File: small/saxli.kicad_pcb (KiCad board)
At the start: 4 copper layers, 160.5 x 102.4 mm, 206 parts, among them IC1 PIC32MX350F256H-V_PT, IC2 SIM808, J1 78800-0001, J10 Conn_01x06_Female, J11 Conn_Coaxial, J12 Conn_Coaxial, J2 Screw_Terminal_01x02, J3 Micro_SD_Card, J4 Conn_01x05_Female, J5 Conn_02x04_Odd_Even, J6 RJ45_Amphenol_RJMG1BD3B8K1ANR, J7 Screw_Terminal_01x08, J8 Screw_Terminal_01x08, J9 Screw_Terminal_01x08, Q1 2N7002, Q2 2N7002, Q3 2N7002, Q4 AO3401A, U1 LM358, U10 TPS5430DDAR, U11 EL357N(C)(TA)-G, U12 EL357N(C)(TA)-G, U13 ASSR-1218, U14 ST485EBDR, U15 ASSR-1218, U16 SRV05-4, U18 ULN2003A, U2 LM7805_TO220, U20 TPS5430DDAR, U4 ENC28J60x-SS, U5 AT25M02, U6 EL357N(C)(TA)-G, U7 EL357N(C)(TA)-G, U8 PCF8563T, U9 ISO1540, Y1 Crystal, Y2 Crystal

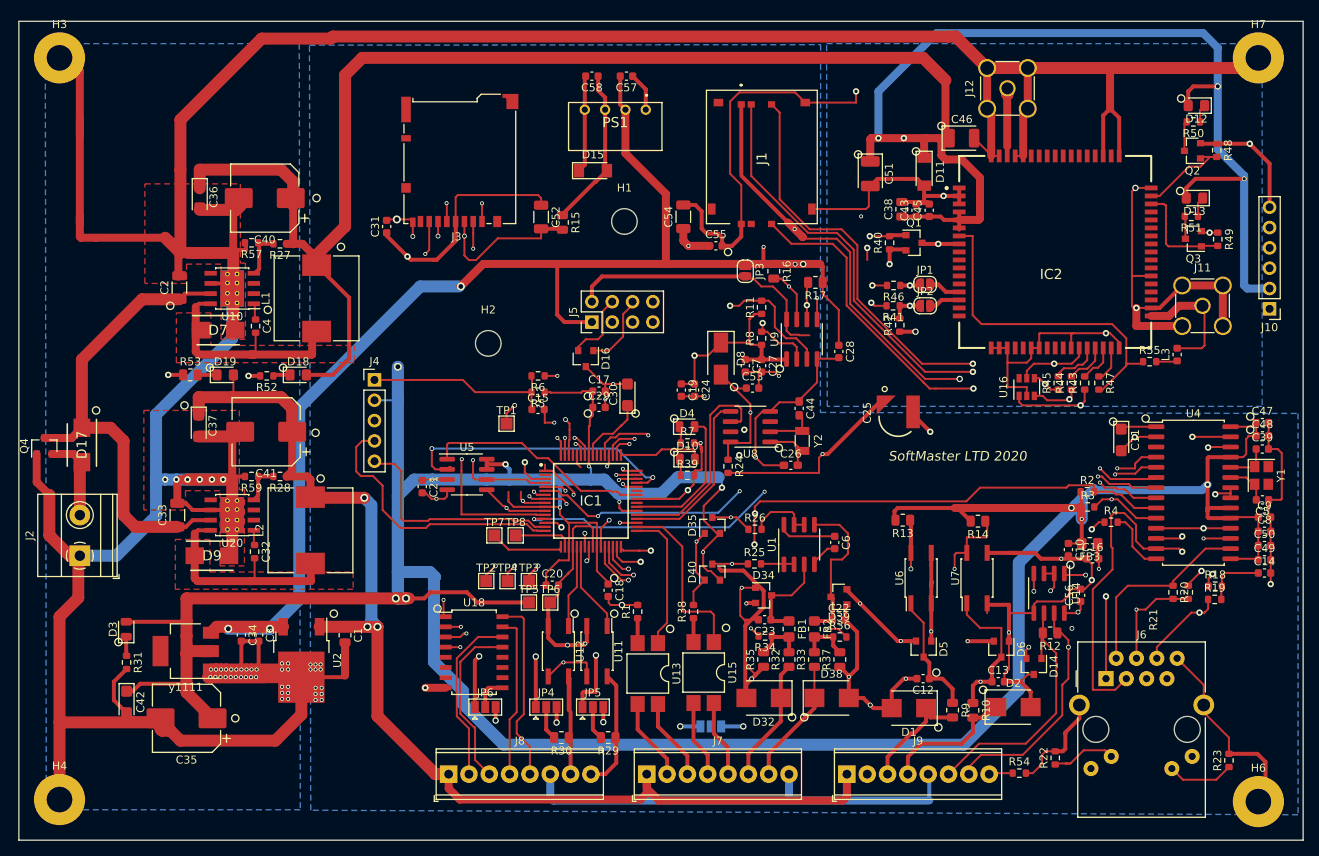
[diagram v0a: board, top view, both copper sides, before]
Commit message: JLCPCB orientation fixed
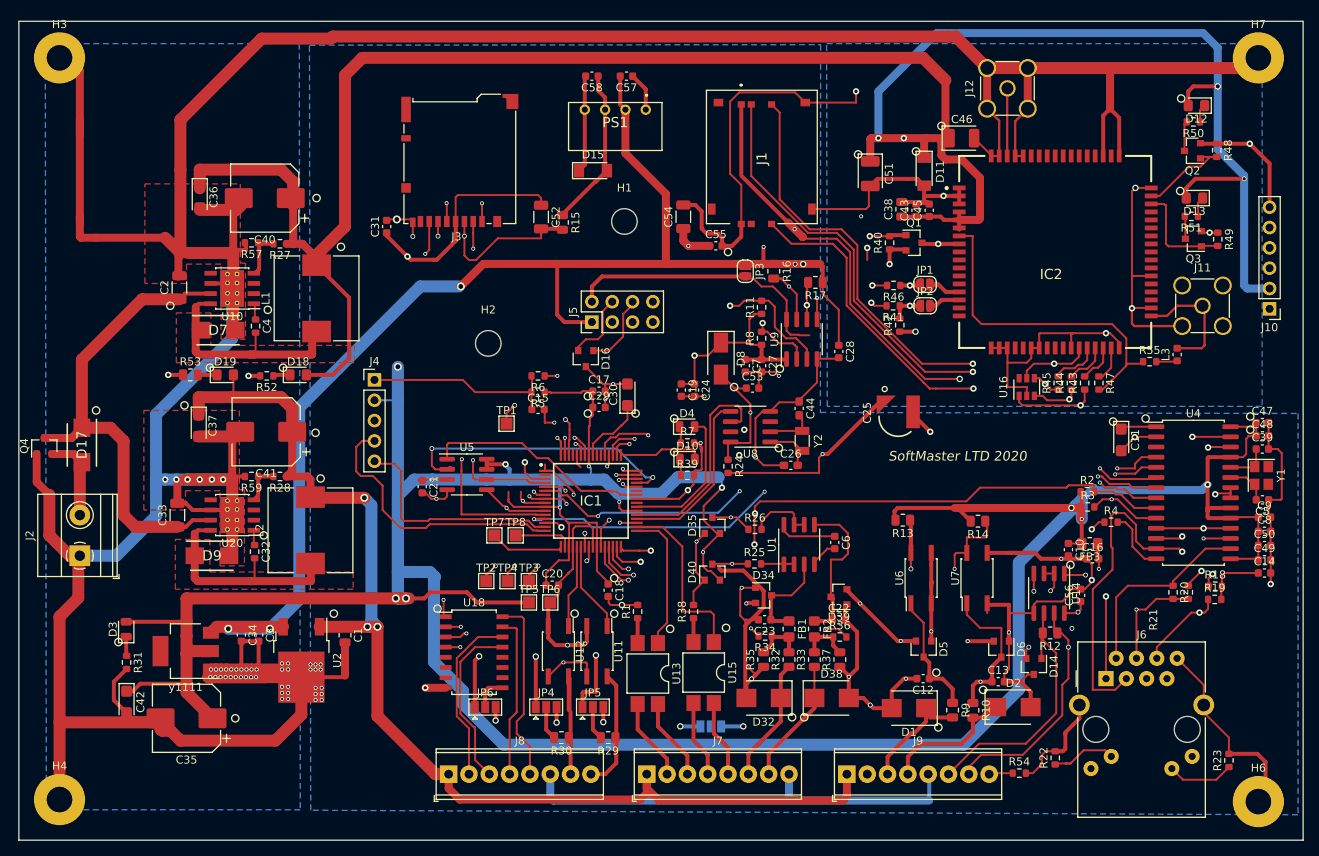
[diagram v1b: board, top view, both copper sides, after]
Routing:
- net GND: track 1217.8 -> 1193.0 mm
- net GSM_ANT: track 15.8 -> 8.46 mm
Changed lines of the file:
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@@
   (general
     (thickness 1.6)
-    (drawings 50)
-    (tracks 2536)
+    (drawings 51)
+    (tracks 2526)
     (zones 0)
     (modules 206)
@@
   (layers
     (0 F.Cu signal)
-    (1 In1.Cu signal)
-    (2 In2.Cu signal)
-    (31 B.Cu signal)
+    (1 In1.Cu signal hide)
+    (2 In2.Cu signal hide)
+    (31 B.Cu signal hide)
     (32 B.Adhes user)
     (33 F.Adhes user)
@@
   )
   (setup
-    (last_trace_width 0.25)
+    (last_trace_width 0.2933)
+    (user_trace_width 0.2933)
     (user_trace_width 0.5)
     (user_trace_width 1)
@@
     )
   )
+  (gr_circle (center 68.707 85.09) (end 68.453 84.709) (layer F.SilkS) (width 0.12))
   (gr_circle (center 133.223 64.262) (end 132.969 63.881) (layer F.SilkS) (width 0.12))
   (gr_circle (center 127.508 66.548) (end 127.254 66.167) (layer F.SilkS) (width 0.12))
@@
   (segment (start 187.833 36.132) (end 185.865 36.132) (width 0.25) (layer F.Cu) (net 1))
   (segment (start 177.785 56.657) (end 177.434 56.657) (width 0.25) (layer F.Cu) (net 1))
-  (via (at 177.785 56.657) (size 0.8) (drill 0.4) (layers F.Cu B.Cu) (net 1))
   (segment (start 162.64 37.657) (end 163.64 37.657) (width 0.25) (layer F.Cu) (net 1))
   (segment (start 149.098 40.526) (end 147.32 40.526) (width 0.5) (layer F.Cu) (net 1))
@@
   (segment (start 106.75 89.859) (end 106.693 89.916) (width 0.25) (layer F.Cu) (net 1))
   (segment (start 163.64 32.575) (end 164.465 31.75) (width 0.5) (layer F.Cu) (net 1))
-  (segment (start 163.64 37.657) (end 163.64 32.575) (width 0.5) (layer F.Cu) (net 1))
-  (segment (start 159.64 32.005) (end 159.385 31.75) (width 0.5) (layer F.Cu) (net 1))
-  (segment (start 159.64 37.657) (end 159.64 32.005) (width 0.5) (layer F.Cu) (net 1))
   (segment (start 177.672 41.657) (end 177.672 41.657) (width 0.25) (layer F.Cu) (net 1))
   (via (at 177.672 41.657) (size 0.8) (drill 0.5) (layers F.Cu B.Cu) (net 1))
@@
   (segment (start 159.131 31.75) (end 159.131 26.67) (width 1) (layer F.Cu) (net 1))
   (segment (start 164.211 31.75) (end 164.211 26.67) (width 1) (layer F.Cu) (net 1))
-  (segment (start 180.706 56.657) (end 183.515 53.848) (width 0.5) (layer F.Cu) (net 1))
-  (segment (start 179.64 56.657) (end 180.706 56.657) (width 0.5) (layer F.Cu) (net 1))
   (segment (start 174.498 31.75) (end 174.498 26.67) (width 1) (layer F.Cu) (net 1))
   (segment (start 173.64 32.608) (end 174.498 31.75) (width 0.5) (layer F.Cu) (net 1))
@@
   (segment (start 142.748 30.988) (end 142.748 29.591) (width 0.25) (layer F.Cu) (net 1))
   (segment (start 136.398 30.988) (end 142.748 30.988) (width 0.25) (layer F.Cu) (net 1))
-  (segment (start 159.64 32.259) (end 159.131 31.75) (width 1) (layer F.Cu) (net 1))
-  (segment (start 159.64 37.657) (end 159.64 32.259) (width 1) (layer F.Cu) (net 1))
-  (segment (start 163.64 32.321) (end 164.211 31.75) (width 1) (layer F.Cu) (net 1))
-  (segment (start 163.64 37.657) (end 163.64 32.321) (width 1) (layer F.Cu) (net 1))
-  (segment (start 177.785 56.657) (end 177.785 58.913) (width 1) (layer F.Cu) (net 1))
-  (segment (start 183.5 58.913) (end 183.515 58.928) (width 1) (layer F.Cu) (net 1))
-  (segment (start 177.785 58.913) (end 183.5 58.913) (width 1) (layer F.Cu) (net 1))
-  (segment (start 183.515 53.848) (end 188.595 53.848) (width 1) (layer F.Cu) (net 1))
-  (segment (start 188.595 53.848) (end 188.595 58.928) (width 1) (layer F.Cu) (net 1))
   (segment (start 107.351 84.292) (end 107.351 86.51) (width 0.25) (layer F.Cu) (net 1))
   (segment (start 107.69049 83.95251) (end 107.351 84.292) (width 0.25) (layer F.Cu) (net 1))
@@
   (segment (start 146.939 51.181) (end 146.939 49.339) (width 0.5) (layer F.Cu) (net 1))
   (via (at 146.939 51.181) (size 0.8) (drill 0.4) (layers F.Cu B.Cu) (net 1))
+  (segment (start 183.515 58.928) (end 177.546 58.928) (width 0.2933) (layer F.Cu) (net 1))
+  (segment (start 177.23301 58.61501) (end 177.23301 56.70099) (width 0.2933) (layer F.Cu) (net 1))
+  (segment (start 177.546 58.928) (end 177.23301 58.61501) (width 0.2933) (layer F.Cu) (net 1))
+  (segment (start 177.23301 56.70099) (end 177.23301 56.45601) (width 0.2933) (layer F.Cu) (net 1))
+  (via (at 177.23301 56.70099) (size 0.8) (drill 0.4) (layers F.Cu B.Cu) (net 1))
+  (segment (start 162.64 33.321) (end 164.211 31.75) (width 0.2933) (layer F.Cu) (net 1))
+  (segment (start 162.64 37.657) (end 162.64 33.321) (width 0.2933) (layer F.Cu) (net 1))
+  (segment (start 160.64 33.259) (end 159.131 31.75) (width 0.2933) (layer F.Cu) (net 1))
+  (segment (start 160.64 37.657) (end 160.64 33.259) (width 0.2933) (layer F.Cu) (net 1))
   (segment (start 57.912 84.025) (end 58.977 84.025) (width 0.5) (layer F.Cu) (net 2))
   (segment (start 58.977 84.025) (end 59.817 83.185) (width 0.5) (layer F.Cu) (net 2))
@@
   (segment (start 150.368 53.848) (end 157.48 60.96) (width 0.5) (layer In1.Cu) (net 182))
   (segment (start 149.479 53.848) (end 150.368 53.848) (width 0.5) (layer In1.Cu) (net 182))
-  (segment (start 161.64 29.495) (end 161.925 29.21) (width 0.5) (layer F.Cu) (net 183))
-  (segment (start 161.64 37.657) (end 161.64 36.48) (width 0.5) (layer F.Cu) (net 183))
-  (segment (start 161.64 36.48) (end 161.64 29.495) (width 0.5) (layer F.Cu) (net 183))
-  (segment (start 161.671 29.972) (end 161.64 30.003) (width 1.5) (layer F.Cu) (net 183))
-  (segment (start 161.671 29.21) (end 161.671 29.972) (width 1.5) (layer F.Cu) (net 183))
-  (segment (start 161.64 36.48) (end 161.64 30.003) (width 1) (layer F.Cu) (net 183))
+  (segment (start 161.64 29.241) (end 161.671 29.21) (width 0.2933) (layer F.Cu) (net 183))
+  (segment (start 161.64 37.657) (end 161.64 29.241) (width 0.2933) (layer F.Cu) (net 183))
   (segment (start 185.737 31.95) (end 186.318 31.369) (width 0.25) (layer F.Cu) (net 184))
   (segment (start 185.737 33.401) (end 185.737 31.95) (width 0.25) (layer F.Cu) (net 184))
@@
   (segment (start 183.912 45.291) (end 183.833 45.212) (width 0.25) (layer F.Cu) (net 194))
   (segment (start 183.912 48.006) (end 183.912 45.291) (width 0.25) (layer F.Cu) (net 194))
-  (segment (start 182.88 61.6965) (end 185.9535 61.6965) (width 0.25) (layer F.Cu) (net 195))
-  (segment (start 185.9535 61.6965) (end 186.309 61.341) (width 0.25) (layer F.Cu) (net 195))
-  (segment (start 186.309 56.642) (end 186.055 56.388) (width 0.25) (layer F.Cu) (net 195))
-  (segment (start 186.309 61.341) (end 186.309 56.642) (width 0.25) (layer F.Cu) (net 195))
-  (segment (start 181.865 57.657) (end 183.134 56.388) (width 1) (layer F.Cu) (net 195))
-  (segment (start 179.64 57.657) (end 181.865 57.657) (width 1) (layer F.Cu) (net 195))
-  (segment (start 183.134 56.388) (end 186.055 56.388) (width 1) (layer F.Cu) (net 195))
+  (segment (start 179.64 57.657) (end 181.611 57.657) (width 0.2933) (layer F.Cu) (net 195))
+  (segment (start 182.88 56.388) (end 186.055 56.388) (width 0.2933) (layer F.Cu) (net 195))
+  (segment (start 181.611 57.657) (end 182.88 56.388) (width 0.2933) (layer F.Cu) (net 195))
+  (segment (start 182.88 61.6965) (end 185.9535 61.6965) (width 0.2933) (layer F.Cu) (net 195))
+  (segment (start 185.9535 61.6965) (end 186.309 61.341) (width 0.2933) (layer F.Cu) (net 195))
+  (segment (start 186.309 56.642) (end 186.055 56.388) (width 0.2933) (layer F.Cu) (net 195))
+  (segment (start 186.309 61.341) (end 186.309 56.642) (width 0.2933) (layer F.Cu) (net 195))
   (segment (start 111.351 86.51) (end 111.351 88.61941) (width 0.25) (layer F.Cu) (net 196))
   (segment (start 114.3 90.678) (end 114.3 90.678) (width 0.25) (layer F.Cu) (net 196))

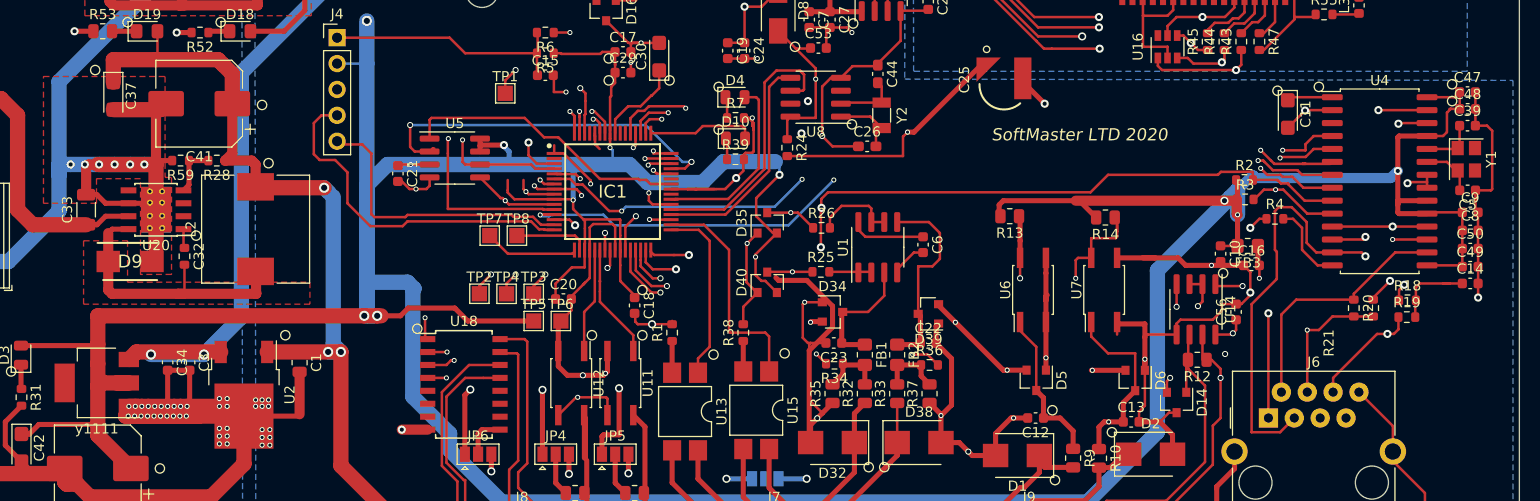
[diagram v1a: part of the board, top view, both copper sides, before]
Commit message: oscillator footprint and capacitors changed
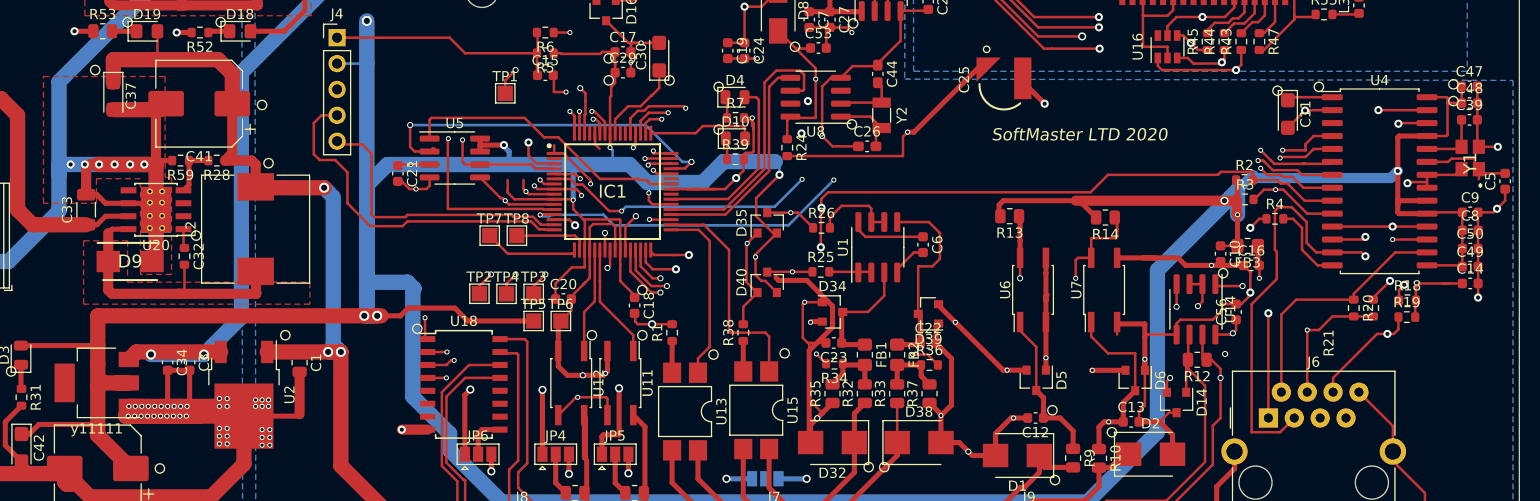
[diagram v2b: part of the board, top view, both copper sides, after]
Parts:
- Y1: value Crystal -> YSX321SL; footprint Crystal:Crystal_SMD_3225-4Pin_3.2x2.5mm -> small:YSX321SL
- moved C5 3.79 mm to (197.2, 79.8), turned to 90 degrees
- moved C39 0.60 mm to (193.7, 73.7)
- moved C47 0.60 mm to (193.7, 70.4)
- moved C48 0.60 mm to (193.7, 72.1)
- moved Y1 0.40 mm to (193.8, 77.5), turned to 90 degrees
- renumbered у1111 to у11111
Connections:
- Y1 pad 1: Net-(C39-Pad1) -> Net-(C5-Pad2)
- Y1 pad 2: Net-(C5-Pad2) -> GND
- Y1 pad 3: (no net) -> Net-(C39-Pad1)
- Y1 pad 4: (no net) -> GND
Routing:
- net Net-(C5-Pad2): track 5.99 -> 9.99 mm
- net GND: track 1193.0 -> 1194.2 mm, vias 95 -> 97
- net Net-(C39-Pad1): track 5.32 -> 6.01 mm
- net VDD3: track 570.8 -> 571.4 mm

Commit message: iso voltage update
minor changes
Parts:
- added JP8: Jumper_NC_Dual, Jumper:SolderJumper-3_P1.3mm_Open_Pad1.0x1.5mm, F.Cu at (122.4, 56.4)
- C39, C5: value 18pF -> 12pF
- JP3: value Jumper -> Jumper_NC_Dual; footprint Jumper:SolderJumper-2_P1.3mm_Open_RoundedPad1.0x1.5mm -> Jumper:SolderJumper-3_P1.3mm_Open_Pad1.0x1.5mm
- R10, R9: value 5k -> 2.2k
- R29, R30: value 2k -> 1k
- moved R16 31.1 mm to (101.6, 56.0)
- moved JP3 24.5 mm to (104.6, 55.5), turned to 90 degrees
- turned R17 to 0 degrees
- renumbered у11111 to у111111
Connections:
- J5 pad 2: 5V_IS -> /communication/5V_IS_OUT
- J5 pad 8: GND_IS -> /communication/GND_IS_OUT
- JP3 pad 2: 5V_IS -> /communication/5V_IS_OUT
- R15 pad 1: GND_IS -> /communication/GND_IS_OUT
- R16 pad 1: VDD5 -> /communication/5V_IS_OUT
- R17 pad 1: VDD5 -> /communication/5V_IS_OUT
- U9 pad 5: GND_IS -> /communication/GND_IS_OUT
- U9 pad 8: 5V_IS -> /communication/5V_IS_OUT
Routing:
- net /communication/GND_IS_OUT: track 0.00 -> 74.9 mm, vias 0 -> 3
- net /communication/5V_IS_OUT: track 0.00 -> 52.6 mm
- net GND_IS: track 94.8 -> 46.5 mm, vias 2 -> 1
- net 5V_IS: track 71.6 -> 37.9 mm, vias 0 -> 1
- net /communication/SDA_ISO: track 39.7 -> 57.1 mm, vias 1 -> 2
- net VDD5: track 412.7 -> 423.5 mm
- net GND: track 1194.2 -> 1196.3 mm, vias 97 -> 98
- net /communication/SCL_ISO: track 37.7 -> 39.2 mm
